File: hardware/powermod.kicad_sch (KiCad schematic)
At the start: 73 parts, among them J1 USB_C_IN, J2 USB_C_OUT, J3 JST_PH_2, J4 STEMMA_QT, J5 UPDI_HDR, Q1 AON7407, Q2 AON7407, Q3 BSS138, SW1 BUTTON, U1 BM8563, U2 ATtiny1616, U3 TPS63020DSJR, U4 TP4056, U5 XC6206P332MR, Y1 32.768kHz

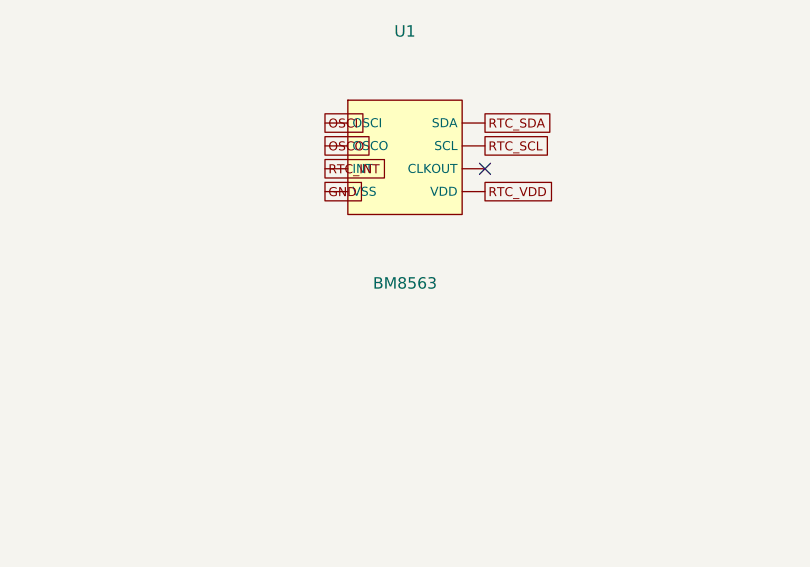
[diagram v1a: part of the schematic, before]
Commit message: hardware: verify LCSC part numbers — two were wrong, now fixed
Checked all 7 audit-list numbers against lcsc.com:
- C2891852 ("ATtiny1616") was actually a 4-pin 1.2mm pin header. Correct
  part is C614136 (ATTINY1616-SN, SOIC-20) — 0 LCSC stock at check time;
  in-stock substitute C145558 (ATTINY1616-SFR) has a 2.7V minimum supply
  (thin margin at battery-empty), so prefer the -SN from Mouser/DigiKey.
- C194063 (BM8563) was the TSSOP-8 package — does not fit the SOIC-8
  footprint — and out of stock. Correct: C269877 (BM8563ESA, SOP-8, ~80k).
- C15483/C382139/C176756/C5446/C52895 all confirmed correct and stocked.

netlist.py LCSC fields corrected; verification table in PREFAB_AUDIT.md.

Co-Authored-By: Claude Opus 4.8 <noreply@anthropic.com>
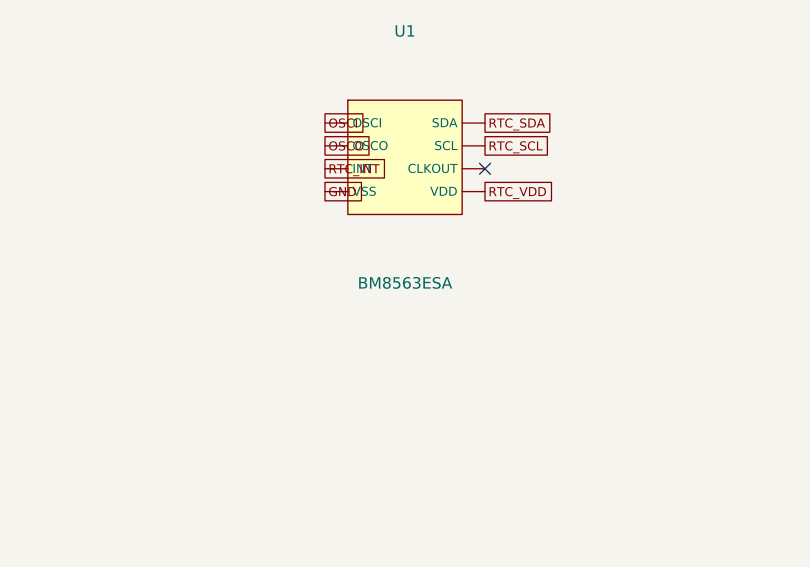
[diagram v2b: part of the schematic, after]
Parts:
- U1: value BM8563 -> BM8563ESA
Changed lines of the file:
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@@
  (symbol (lib_id "powermod:PM_U1") (at 670.5600000000001 294.64000000000004 0) (unit 1) (in_bom yes) (on_board yes)
   (property "Reference" "U1" (at 670.5600000000001 280.64000000000004 0) (effects (font (size 1.27 1.27))))
-  (property "Value" "BM8563" (at 670.5600000000001 308.64000000000004 0) (effects (font (size 1.27 1.27))))
+  (property "Value" "BM8563ESA" (at 670.5600000000001 308.64000000000004 0) (effects (font (size 1.27 1.27))))
   (property "Footprint" "Package_SO:SOIC-8_3.9x4.9mm_P1.27mm" (at 670.5600000000001 294.64000000000004 0) (effects (font (size 1.27 1.27)) hide))
   (pin "1")

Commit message: hardware: commit LED + crystal BOM parts (both in-stock, verified)
Crystal Y1: Epson Q13FC13500004 (LCSC C32346, ~286k stock) — 32.768kHz
CL=12.5pF matching the BM8563. Netlist-only (footprint unchanged).

LEDs D1/D2: TOGIALED TJ-S3227 (LCSC C601677, ~7.7k stock), yellow-green die
fixes the dim-green issue. Its pinout is the OPPOSITE numbering to the stock
KiCad Avago PLCC4 (would reverse polarity), so a local footprint was built
from LCSC's EasyEDA model (2 independent diodes, anodes=pins 2/3,
cathodes=pins 1/4). D1/D2 swapped on the board and anodes re-routed; cathodes
tie through the GND pour. Board rebuilt at rot 0 (anodes stacked under the
resistors, no crossing). LED_SMD lib dropped (both LEDs now in powermod lib).

Verified: pad-diff 214/214 + 11 NC, 0 unconnected, 0 clearance, only the 4
intrinsic U3 QFN-neck track_width flags. Red/green die identity is
firmware-adjustable (documented in PREFAB_AUDIT.md).

Co-Authored-By: Claude Opus 4.8 <noreply@anthropic.com>
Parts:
- D1, D2: value LED_RG_PLCC4 -> TJ-S3227; footprint LED_SMD:LED_Avago_PLCC4_3.2x2.8mm_CW -> powermod:LED_TJ-S3227_RG_3.2x2.7mm
- Y1: value 32.768kHz -> Q13FC13500004
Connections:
- net D1_GRN: now also D1.2 (A_GRN); no longer D1.3 (A_GRN)
- net D1_RED: now also D1.3 (A_RED); no longer D1.1 (A_RED)
- net D2_GRN: now also D2.2 (A_GRN); no longer D2.3 (A_GRN)
- net D2_RED: now also D2.3 (A_RED); no longer D2.1 (A_RED)
- net GND: now also D1.1 (K_GRN), D2.1 (K_GRN); no longer D1.2 (K_RED), D2.2 (K_RED)
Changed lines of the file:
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@@
  (symbol (lib_id "powermod:PM_D1") (at 172.72 162.56 0) (unit 1) (in_bom yes) (on_board yes)
   (property "Reference" "D1" (at 172.72 148.56 0) (effects (font (size 1.27 1.27))))
-  (property "Value" "LED_RG_PLCC4" (at 172.72 176.56 0) (effects (font (size 1.27 1.27))))
-  (property "Footprint" "LED_SMD:LED_Avago_PLCC4_3.2x2.8mm_CW" (at 172.72 162.56 0) (effects (font (size 1.27 1.27)) hide))
+  (property "Value" "TJ-S3227" (at 172.72 176.56 0) (effects (font (size 1.27 1.27))))
+  (property "Footprint" "powermod:LED_TJ-S3227_RG_3.2x2.7mm" (at 172.72 162.56 0) (effects (font (size 1.27 1.27)) hide))
   (pin "1")
   (pin "2")
@@
  (symbol (lib_id "powermod:PM_D2") (at 172.72 228.6 0) (unit 1) (in_bom yes) (on_board yes)
   (property "Reference" "D2" (at 172.72 214.6 0) (effects (font (size 1.27 1.27))))
-  (property "Value" "LED_RG_PLCC4" (at 172.72 242.6 0) (effects (font (size 1.27 1.27))))
-  (property "Footprint" "LED_SMD:LED_Avago_PLCC4_3.2x2.8mm_CW" (at 172.72 228.6 0) (effects (font (size 1.27 1.27)) hide))
+  (property "Value" "TJ-S3227" (at 172.72 242.6 0) (effects (font (size 1.27 1.27))))
+  (property "Footprint" "powermod:LED_TJ-S3227_RG_3.2x2.7mm" (at 172.72 228.6 0) (effects (font (size 1.27 1.27)) hide))
   (pin "1")
   (pin "2")
@@
  (symbol (lib_id "powermod:PM_Y1") (at 741.6800000000001 162.56 0) (unit 1) (in_bom yes) (on_board yes)
   (property "Reference" "Y1" (at 741.6800000000001 148.56 0) (effects (font (size 1.27 1.27))))
-  (property "Value" "32.768kHz" (at 741.6800000000001 176.56 0) (effects (font (size 1.27 1.27))))
+  (property "Value" "Q13FC13500004" (at 741.6800000000001 176.56 0) (effects (font (size 1.27 1.27))))
   (property "Footprint" "Crystal:Crystal_SMD_3215-2Pin_3.2x1.5mm" (at 741.6800000000001 162.56 0) (effects (font (size 1.27 1.27)) hide))
   (pin "1")
@@
  (global_label "3V3" (shape passive) (at 166.37 96.52000000000001 0) (effects (font (size 1.0 1.0)) (justify left)))
  (global_label "GND" (shape passive) (at 179.07 96.52000000000001 0) (effects (font (size 1.0 1.0)) (justify left)))
- (global_label "D1_RED" (shape passive) (at 163.82999999999998 161.29 0) (effects (font (size 1.0 1.0)) (justify left)))
- (global_label "GND" (shape passive) (at 163.82999999999998 163.83 0) (effects (font (size 1.0 1.0)) (justify left)))
- (global_label "D1_GRN" (shape passive) (at 181.61 161.29 0) (effects (font (size 1.0 1.0)) (justify left)))
+ (global_label "GND" (shape passive) (at 163.82999999999998 161.29 0) (effects (font (size 1.0 1.0)) (justify left)))
+ (global_label "D1_GRN" (shape passive) (at 163.82999999999998 163.83 0) (effects (font (size 1.0 1.0)) (justify left)))
+ (global_label "D1_RED" (shape passive) (at 181.61 161.29 0) (effects (font (size 1.0 1.0)) (justify left)))
  (global_label "GND" (shape passive) (at 181.61 163.83 0) (effects (font (size 1.0 1.0)) (justify left)))
- (global_label "D2_RED" (shape passive) (at 163.82999999999998 227.32999999999998 0) (effects (font (size 1.0 1.0)) (justify left)))
- (global_label "GND" (shape passive) (at 163.82999999999998 229.87 0) (effects (font (size 1.0 1.0)) (justify left)))
- (global_label "D2_GRN" (shape passive) (at 181.61 227.32999999999998 0) (effects (font (size 1.0 1.0)) (justify left)))
+ (global_label "GND" (shape passive) (at 163.82999999999998 227.32999999999998 0) (effects (font (size 1.0 1.0)) (justify left)))
+ (global_label "D2_GRN" (shape passive) (at 163.82999999999998 229.87 0) (effects (font (size 1.0 1.0)) (justify left)))
+ (global_label "D2_RED" (shape passive) (at 181.61 227.32999999999998 0) (effects (font (size 1.0 1.0)) (justify left)))
  (global_label "GND" (shape passive) (at 181.61 229.87 0) (effects (font (size 1.0 1.0)) (justify left)))
  (global_label "RTC_VDD" (shape passive) (at 166.37 294.64000000000004 0) (effects (font (size 1.0 1.0)) (justify left)))

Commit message: hardware: swap MCU ATtiny1616 -> PY32F003F18P6 (netlist)
No well-stocked AVR exists at JLC in any package (whole tinyAVR/megaAVR-0 line
<~100 units, all Extended, verified 2026-07-18). PY32F003F18P6 (ARM M0+,
TSSOP-20, LCSC C5379864, ~22k stock) is in-stock, cheaper, and stays out of QFN.

- U2: TSSOP-20 pinout transcribed + verified vs LCSC C5379864 symbol. ADC on
  PA4/PA5, HW I2C1 on PB6/PB7 (STEMMA), RTC I2C bit-banged on PF0/PF1, SWD on
  PA13/PA14 shared with the 2 BAT LEDs (connect-under-reset via NRST=PF2),
  BOOT0=PF4 carries an LED output. 0 spare pins. Net names unchanged vs the
  ATtiny map (only pin assignment moved); UPDI dropped, NRST added.
- Dividers UNCHANGED: with VDD (3.3V) ADC ref the 1M/330k pair peaks at
  1.30V/1.05V (no clip) at finer resolution than the ATtiny's 10-bit.
- J5: 3-pin UPDI header -> 1x05 SWD header (GND/SWCLK/SWDIO/NRST/3V3).
- self-test + validate() pass: 73 components, 227 pins, 45 nets.

Board footprint swap + MCU-area re-route still pending (does NOT touch the
hand-routed power/USB sections).

Co-Authored-By: Claude Opus 4.8 <noreply@anthropic.com>
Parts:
- J5: value UPDI_HDR -> SWD_HDR; footprint Connector_PinHeader_2.54mm:PinHeader_1x03_P2.54mm_Vertical -> Connector_PinHeader_2.54mm:PinHeader_1x05_P2.54mm_Vertical
- U2: value ATtiny1616 -> PY32F003F18P6; footprint Package_SO:SOIC-20W_7.5x12.8mm_P1.27mm -> Package_SO:TSSOP-20_4.4x6.5mm_P0.65mm
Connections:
- net 3V3: now also J5.5 (3V3), U2.9 (VDD); no longer J5.2 (3V3), U2.1 (VCC)
- net BUTTON: now also U2.20 (PA1/BUTTON); no longer U2.18 (PA2/BUTTON)
- net CHG_CE: now also U2.5 (PA6/CHG_CE); no longer U2.12 (PC0/CHG_CE)
- net CHG_CHRG: now also U2.12 (PB5/CHG_CHRG); no longer U2.7 (PB4/CHG_CHRG)
- net CONV_EN: now also U2.2 (PA3/CONV_EN); no longer U2.19 (PA3/CONV_EN)
- net GND: now also J5.1 (GND), U2.7 (VSS); no longer J5.3 (GND), U2.20 (GND)
- net LED_BAT_A: now also J5.3 (SWDIO), U2.10 (PA13/SWDIO/LED_BAT_A); no longer U2.4 (PA6/LED_BAT_A)
- net LED_BAT_B: now also J5.2 (SWCLK), U2.11 (PA14/SWCLK/LED_BAT_B); no longer U2.5 (PA7/LED_BAT_B)
- net LED_PWR_A: now also U2.19 (PA0/LED_PWR_A); no longer U2.9 (PB2/LED_PWR_A)
- net LED_PWR_B: now also U2.15 (PF4/BOOT0/LED_PWR_B); no longer U2.8 (PB3/LED_PWR_B)
- net Q1_GATE_DRV: now also U2.1 (PA2/Q1_GATE_DRV); no longer U2.15 (PC3/Q1_GATE_DRV)
- net RTC_INT: now also U2.8 (PA12/RTC_INT); no longer U2.14 (PC2/RTC_INT)
- net RTC_SCL: now also U2.17 (PF1/RTC_SCL); no longer U2.13 (PC1/RTC_SCL)
- net RTC_SDA: now also U2.16 (PF0/RTC_SDA); no longer U2.17 (PA1/RTC_SDA)
- net SCL: now also U2.13 (PB6/I2C_SCL); no longer U2.11 (PB0/SCL)
- net SDA: now also U2.14 (PB7/I2C_SDA); no longer U2.10 (PB1/SDA)
- net VBAT_DIV: now also U2.3 (PA4/VBAT_SENSE); no longer U2.2 (PA4/VBAT_SENSE)
- net VBUS_DIV: now also U2.4 (PA5/VBUS_SENSE); no longer U2.3 (PA5/VBUS_SENSE)
- removed net UPDI: J5.1 (UPDI), U2.16 (PA0/UPDI)
- new net NRST: J5.4 (NRST), U2.18 (PF2/NRST)
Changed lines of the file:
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@@
  (symbol (lib_id "powermod:PM_J5") (at 243.84 294.64000000000004 0) (unit 1) (in_bom yes) (on_board yes)
   (property "Reference" "J5" (at 243.84 280.64000000000004 0) (effects (font (size 1.27 1.27))))
-  (property "Value" "UPDI_HDR" (at 243.84 308.64000000000004 0) (effects (font (size 1.27 1.27))))
-  (property "Footprint" "Connector_PinHeader_2.54mm:PinHeader_1x03_P2.54mm_Vertical" (at 243.84 294.64000000000004 0) (effects (font (size 1.27 1.27)) hide))
-  (pin "1")
-  (pin "2")
-  (pin "3"))
+  (property "Value" "SWD_HDR" (at 243.84 308.64000000000004 0) (effects (font (size 1.27 1.27))))
+  (property "Footprint" "Connector_PinHeader_2.54mm:PinHeader_1x05_P2.54mm_Vertical" (at 243.84 294.64000000000004 0) (effects (font (size 1.27 1.27)) hide))
+  (pin "1")
+  (pin "2")
+  (pin "3")
+  (pin "4")
+  (pin "5"))
  (symbol (lib_id "powermod:PM_JP1") (at 243.84 360.68000000000006 0) (unit 1) (in_bom yes) (on_board yes)
   (property "Reference" "JP1" (at 243.84 346.68000000000006 0) (effects (font (size 1.27 1.27))))
@@
  (symbol (lib_id "powermod:PM_U2") (at 670.5600000000001 360.68000000000006 0) (unit 1) (in_bom yes) (on_board yes)
   (property "Reference" "U2" (at 670.5600000000001 346.68000000000006 0) (effects (font (size 1.27 1.27))))
-  (property "Value" "ATtiny1616" (at 670.5600000000001 374.68000000000006 0) (effects (font (size 1.27 1.27))))
-  (property "Footprint" "Package_SO:SOIC-20W_7.5x12.8mm_P1.27mm" (at 670.5600000000001 360.68000000000006 0) (effects (font (size 1.27 1.27)) hide))
+  (property "Value" "PY32F003F18P6" (at 670.5600000000001 374.68000000000006 0) (effects (font (size 1.27 1.27))))
+  (property "Footprint" "Package_SO:TSSOP-20_4.4x6.5mm_P0.65mm" (at 670.5600000000001 360.68000000000006 0) (effects (font (size 1.27 1.27)) hide))
   (pin "1")
   (pin "2")
@@
  (global_label "SDA" (shape passive) (at 252.73000000000002 227.32999999999998 0) (effects (font (size 1.0 1.0)) (justify left)))
  (global_label "SCL" (shape passive) (at 252.73000000000002 229.87 0) (effects (font (size 1.0 1.0)) (justify left)))
- (global_label "UPDI" (shape passive) (at 234.95 293.37000000000006 0) (effects (font (size 1.0 1.0)) (justify left)))
- (global_label "3V3" (shape passive) (at 234.95 295.91 0) (effects (font (size 1.0 1.0)) (justify left)))
- (global_label "GND" (shape passive) (at 252.73000000000002 293.37000000000006 0) (effects (font (size 1.0 1.0)) (justify left)))
+ (global_label "GND" (shape passive) (at 234.95 292.1 0) (effects (font (size 1.0 1.0)) (justify left)))
+ (global_label "LED_BAT_B" (shape passive) (at 234.95 294.64000000000004 0) (effects (font (size 1.0 1.0)) (justify left)))
+ (global_label "LED_BAT_A" (shape passive) (at 234.95 297.18000000000006 0) (effects (font (size 1.0 1.0)) (justify left)))
+ (global_label "NRST" (shape passive) (at 252.73000000000002 292.1 0) (effects (font (size 1.0 1.0)) (justify left)))
+ (global_label "3V3" (shape passive) (at 252.73000000000002 294.64000000000004 0) (effects (font (size 1.0 1.0)) (justify left)))
  (global_label "CHG_JPD" (shape passive) (at 237.49 360.68000000000006 0) (effects (font (size 1.0 1.0)) (justify left)))
  (global_label "VBACKUP" (shape passive) (at 250.19 360.68000000000006 0) (effects (font (size 1.0 1.0)) (justify left)))
@@
  (global_label "RTC_SCL" (shape passive) (at 679.45 293.37000000000006 0) (effects (font (size 1.0 1.0)) (justify left)))
  (global_label "RTC_VDD" (shape passive) (at 679.45 298.45000000000005 0) (effects (font (size 1.0 1.0)) (justify left)))
- (global_label "3V3" (shape passive) (at 661.6700000000001 349.25000000000006 0) (effects (font (size 1.0 1.0)) (justify left)))
- (global_label "VBAT_DIV" (shape passive) (at 661.6700000000001 351.7900000000001 0) (effects (font (size 1.0 1.0)) (justify left)))
- (global_label "VBUS_DIV" (shape passive) (at 661.6700000000001 354.33000000000004 0) (effects (font (size 1.0 1.0)) (justify left)))
- (global_label "LED_BAT_A" (shape passive) (at 661.6700000000001 356.87000000000006 0) (effects (font (size 1.0 1.0)) (justify left)))
- (global_label "LED_BAT_B" (shape passive) (at 661.6700000000001 359.4100000000001 0) (effects (font (size 1.0 1.0)) (justify left)))
+ (global_label "Q1_GATE_DRV" (shape passive) (at 661.6700000000001 349.25000000000006 0) (effects (font (size 1.0 1.0)) (justify left)))
+ (global_label "CONV_EN" (shape passive) (at 661.6700000000001 351.7900000000001 0) (effects (font (size 1.0 1.0)) (justify left)))
+ (global_label "VBAT_DIV" (shape passive) (at 661.6700000000001 354.33000000000004 0) (effects (font (size 1.0 1.0)) (justify left)))
+ (global_label "VBUS_DIV" (shape passive) (at 661.6700000000001 356.87000000000006 0) (effects (font (size 1.0 1.0)) (justify left)))
+ (global_label "CHG_CE" (shape passive) (at 661.6700000000001 359.4100000000001 0) (effects (font (size 1.0 1.0)) (justify left)))
  (global_label "CHG_STDBY" (shape passive) (at 661.6700000000001 361.95000000000005 0) (effects (font (size 1.0 1.0)) (justify left)))
- (global_label "CHG_CHRG" (shape passive) (at 661.6700000000001 364.49000000000007 0) (effects (font (size 1.0 1.0)) (justify left)))
- (global_label "LED_PWR_B" (shape passive) (at 661.6700000000001 367.0300000000001 0) (effects (font (size 1.0 1.0)) (justify left)))
- (global_label "LED_PWR_A" (shape passive) (at 661.6700000000001 369.57000000000005 0) (effects (font (size 1.0 1.0)) (justify left)))
- (global_label "SDA" (shape passive) (at 661.6700000000001 372.11000000000007 0) (effects (font (size 1.0 1.0)) (justify left)))
- (global_label "SCL" (shape passive) (at 679.45 349.25000000000006 0) (effects (font (size 1.0 1.0)) (justify left)))
- (global_label "CHG_CE" (shape passive) (at 679.45 351.7900000000001 0) (effects (font (size 1.0 1.0)) (justify left)))
- (global_label "RTC_SCL" (shape passive) (at 679.45 354.33000000000004 0) (effects (font (size 1.0 1.0)) (justify left)))
- (global_label "RTC_INT" (shape passive) (at 679.45 356.87000000000006 0) (effects (font (size 1.0 1.0)) (justify left)))
- (global_label "Q1_GATE_DRV" (shape passive) (at 679.45 359.4100000000001 0) (effects (font (size 1.0 1.0)) (justify left)))
- (global_label "UPDI" (shape passive) (at 679.45 361.95000000000005 0) (effects (font (size 1.0 1.0)) (justify left)))
- (global_label "RTC_SDA" (shape passive) (at 679.45 364.49000000000007 0) (effects (font (size 1.0 1.0)) (justify left)))
- (global_label "BUTTON" (shape passive) (at 679.45 367.0300000000001 0) (effects (font (size 1.0 1.0)) (justify left)))
- (global_label "CONV_EN" (shape passive) (at 679.45 369.57000000000005 0) (effects (font (size 1.0 1.0)) (justify left)))
- (global_label "GND" (shape passive) (at 679.45 372.11000000000007 0) (effects (font (size 1.0 1.0)) (justify left)))
+ (global_label "GND" (shape passive) (at 661.6700000000001 364.49000000000007 0) (effects (font (size 1.0 1.0)) (justify left)))
+ (global_label "RTC_INT" (shape passive) (at 661.6700000000001 367.0300000000001 0) (effects (font (size 1.0 1.0)) (justify left)))
+ (global_label "3V3" (shape passive) (at 661.6700000000001 369.57000000000005 0) (effects (font (size 1.0 1.0)) (justify left)))
+ (global_label "LED_BAT_A" (shape passive) (at 661.6700000000001 372.11000000000007 0) (effects (font (size 1.0 1.0)) (justify left)))
+ (global_label "LED_BAT_B" (shape passive) (at 679.45 349.25000000000006 0) (effects (font (size 1.0 1.0)) (justify left)))
+ (global_label "CHG_CHRG" (shape passive) (at 679.45 351.7900000000001 0) (effects (font (size 1.0 1.0)) (justify left)))
+ (global_label "SCL" (shape passive) (at 679.45 354.33000000000004 0) (effects (font (size 1.0 1.0)) (justify left)))
+ (global_label "SDA" (shape passive) (at 679.45 356.87000000000006 0) (effects (font (size 1.0 1.0)) (justify left)))
+ (global_label "LED_PWR_B" (shape passive) (at 679.45 359.4100000000001 0) (effects (font (size 1.0 1.0)) (justify left)))
+ (global_label "RTC_SDA" (shape passive) (at 679.45 361.95000000000005 0) (effects (font (size 1.0 1.0)) (justify left)))
+ (global_label "RTC_SCL" (shape passive) (at 679.45 364.49000000000007 0) (effects (font (size 1.0 1.0)) (justify left)))
+ (global_label "NRST" (shape passive) (at 679.45 367.0300000000001 0) (effects (font (size 1.0 1.0)) (justify left)))
+ (global_label "LED_PWR_A" (shape passive) (at 679.45 369.57000000000005 0) (effects (font (size 1.0 1.0)) (justify left)))
+ (global_label "BUTTON" (shape passive) (at 679.45 372.11000000000007 0) (effects (font (size 1.0 1.0)) (justify left)))
  (global_label "VSYS" (shape passive) (at 661.6700000000001 417.83000000000004 0) (effects (font (size 1.0 1.0)) (justify left)))
  (global_label "GND" (shape passive) (at 661.6700000000001 420.37 0) (effects (font (size 1.0 1.0)) (justify left)))

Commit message: hardware: board footprint swap for PY32F003 (U2 TSSOP-20, J5 SWD, TP7 NRST)
Text-level swap on powermod.kicad_pcb (pcbnew footprint mutation segfaults):
- U2 SOIC-20W -> TSSOP-20_4.4x6.5mm, 20 pads net-assigned to the PY32 pinmap
- J5 3-pin UPDI -> 3-pin SWD (GND/SWCLK/SWDIO); a 5-pin header won't fit the
  packed RTC/USB corner, so NRST is exposed on the new TP7 probe pad instead
- stripped 201 stale MCU-net segments + 6 local 3V3/GND stubs
Verified in pcbnew: correct nets, zero courtyard collisions. DRC clean apart
from the 4 known U3 track_width necks + 36 unrouted MCU connections (ratsnest).
MCU-area routing still to do; power/USB/charger routing untouched.

Co-Authored-By: Claude Opus 4.8 <noreply@anthropic.com>
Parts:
- added TP7: NRST_PAD, TestPoint:TestPoint_Pad_2.0x2.0mm, symbol powermod:PM_TP7
- J5: footprint Connector_PinHeader_2.54mm:PinHeader_1x05_P2.54mm_Vertical -> Connector_PinHeader_2.54mm:PinHeader_1x03_P2.54mm_Vertical
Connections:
- net 3V3: no longer J5.5 (3V3)
- net NRST: now also TP7.1 (P); no longer J5.4 (NRST)
